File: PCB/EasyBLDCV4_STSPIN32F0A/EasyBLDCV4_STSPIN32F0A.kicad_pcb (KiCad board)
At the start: 4 copper layers, 72.4 x 45.7 mm, 74 parts, among them J1 10159560-A00221RLF, J2 Conn_01x05_Pin, Q1 CSD17573Q5B, Q2 CSD17573Q5B, Q3 CSD17573Q5B, Q4 CSD17573Q5B, Q5 CSD17573Q5B, Q6 CSD17573Q5B, U1 MCF8329A1IREER

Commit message: Started Layout
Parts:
- removed JP1, JP2: SolderJumper_3_Bridged12, Jumper:SolderJumper-3_P1.3mm_Bridged12_RoundedPad1.0x1.5mm_NumberLabels
- removed Q4, Q5, Q6: CSD17573Q5B, EasyBLDC:DNK0008A
- removed TP10, TP11, TP12, TP13, TP14, TP15, TP16, TP3, TP4, TP5, TP6, TP7, TP8, TP9: TestPoint, TestPoint:TestPoint_Pad_D1.5mm
- added C19: 1u, Capacitor_SMD:C_0402_1005Metric, F.Cu at (163.3, 76.5)
- added C20: 1u, Capacitor_SMD:C_0402_1005Metric, F.Cu at (161.3, 76.5)
- added C21: 1u, Capacitor_SMD:C_0402_1005Metric, F.Cu at (159.3, 76.5)
- added D4: GREEN, LED_SMD:LED_0603_1608Metric, F.Cu at (133.1, 102.3)
- added L1: 22u, Inductor_SMD:L_0805_2012Metric, F.Cu at (153.0, 61.0)
- added R23: 10k, Resistor_SMD:R_0402_1005Metric, F.Cu at (155.3, 71.2)
- added U2: STSPIN32F0A, EasyBLDC:IC_STSPIN32F0A, F.Cu at (161.2, 70.8)
- C1: value 10u -> 47u; footprint Capacitor_SMD:CP_Elec_5x5.3 -> Capacitor_SMD:C_1206_3216Metric
- C10, C11, C9: value 1u -> 47u; footprint Capacitor_SMD:C_0603_1608Metric -> Capacitor_SMD:C_1206_3216Metric
- C12: footprint Capacitor_SMD:C_0603_1608Metric -> Capacitor_SMD:C_0805_2012Metric
- C13: value 0.1u -> 100n; footprint Capacitor_SMD:C_0603_1608Metric -> Capacitor_SMD:C_0402_1005Metric
- C14: value 470n -> 22u
- C15: value 1u -> 100n; footprint Capacitor_SMD:C_0603_1608Metric -> Capacitor_SMD:C_0402_1005Metric
- C16: value 10u -> 100n; footprint Capacitor_SMD:C_0603_1608Metric -> Capacitor_SMD:C_0402_1005Metric
- C17: value 10u -> 100n; footprint Capacitor_SMD:C_2220_5750Metric -> Capacitor_SMD:C_0402_1005Metric
- C18: footprint Capacitor_SMD:C_0603_1608Metric -> Capacitor_SMD:C_0402_1005Metric
- C2: value 220u -> 47u; footprint Capacitor_SMD:CP_Elec_10x10.5 -> Capacitor_SMD:C_1206_3216Metric
- C3, C7: value 0.01u -> 47u; footprint Capacitor_SMD:C_0805_2012Metric -> Capacitor_SMD:C_1206_3216Metric
- C4: value 4.7u -> 100n; footprint Capacitor_SMD:C_1210_3225Metric -> Capacitor_SMD:C_0402_1005Metric
- C5: value 0.01u -> 100n; footprint Capacitor_SMD:C_0805_2012Metric -> Capacitor_SMD:C_0402_1005Metric
- C6, C8: value 4.7u -> 47u; footprint Capacitor_SMD:C_1210_3225Metric -> Capacitor_SMD:C_1206_3216Metric
- D1, D2: value GREEN -> D; footprint LED_SMD:LED_0805_2012Metric -> Diode_SMD:D_0402_1005Metric
- D3: value RED -> GREEN; footprint LED_SMD:LED_0805_2012Metric -> LED_SMD:LED_0603_1608Metric
- J2: value Conn_01x05_Pin -> STLINK-V3MINIE-EDGE; footprint Connector_PinSocket_2.54mm:PinSocket_1x05_P2.54mm_Vertical -> EasyBLDC:STLINK-V3MINIE-EDGE
- Q1, Q2, Q3: value CSD17573Q5B -> IAUC60N04S6N031HATMA1; footprint EasyBLDC:DNK0008A -> EasyBLDC:PG-TDSON-8-56
- R1, R2, R3, R4: value 10k -> 33; footprint Resistor_SMD:R_0603_1608Metric -> Resistor_SMD:R_0402_1005Metric
- R10: value 10 -> 1k; footprint Resistor_SMD:R_0603_1608Metric -> Resistor_SMD:R_0402_1005Metric
- R11, R13, R18: value 0 -> 10k; footprint Resistor_SMD:R_0603_1608Metric -> Resistor_SMD:R_0402_1005Metric
- R12: value 0.001 -> 10k; footprint Resistor_SMD:R_2512_6332Metric -> Resistor_SMD:R_0402_1005Metric
- R14: value 5.1k -> 0.001; footprint Resistor_SMD:R_0603_1608Metric -> Resistor_SMD:R_2512_6332Metric
- R15, R17: value 5.1k -> 2.2k; footprint Resistor_SMD:R_0603_1608Metric -> Resistor_SMD:R_0402_1005Metric
- R16: value 0 -> 2.2k; footprint Resistor_SMD:R_0603_1608Metric -> Resistor_SMD:R_0402_1005Metric
- R19: value 5.1k -> 1k; footprint Resistor_SMD:R_0603_1608Metric -> Resistor_SMD:R_0402_1005Metric
- R20: value 2k -> 100k; footprint Resistor_SMD:R_0603_1608Metric -> Resistor_SMD:R_0402_1005Metric
- R21: value 890 -> 10k; footprint Resistor_SMD:R_0603_1608Metric -> Resistor_SMD:R_0201_0603Metric
- R22: value 890 -> 2.2k; footprint Resistor_SMD:R_0603_1608Metric -> Resistor_SMD:R_0201_0603Metric
- R5, R6: value 10 -> 33; footprint Resistor_SMD:R_0603_1608Metric -> Resistor_SMD:R_0402_1005Metric
- R7, R8, R9: value 10 -> 10k; footprint Resistor_SMD:R_0603_1608Metric -> Resistor_SMD:R_0402_1005Metric
- TP1: value TestPoint -> TELEMETRY; footprint TestPoint:TestPoint_Pad_D1.5mm -> TestPoint:TestPoint_Pad_D3.0mm
- TP2: footprint TestPoint:TestPoint_Pad_D1.5mm -> TestPoint:TestPoint_Pad_D3.0mm
- U1: value MCF8329A1IREER -> INA180A1IDBVR; footprint EasyBLDC:WQFN36_REE_TEX -> EasyBLDC:DBV0005A_N
- moved R2 136.5 mm to (158.8, 91.0)
- moved R14 132.6 mm to (164.0, 99.5)
- moved R4 131.9 mm to (157.2, 78.2), turned to 0 degrees
- moved J2 128.5 mm to (176.5, 65.5)
- moved C14 127.7 mm to (167.2, 75.2), turned to -90 degrees
- moved C15 127.6 mm to (167.3, 67.0), turned to 0 degrees
- moved C17 127.5 mm to (160.5, 63.5)
- moved D1 125.4 mm to (159.2, 63.5), turned to 90 degrees
- moved R18 122.4 mm to (167.3, 72.0), turned to 180 degrees
- moved R16 122.1 mm to (166.8, 63.5)
- moved C18 122.0 mm to (163.0, 63.5), turned to -90 degrees
- moved R20 121.6 mm to (155.3, 70.0), turned to 0 degrees
- moved C13 121.0 mm to (161.8, 63.5), turned to 90 degrees
- moved U1 120.4 mm to (157.4, 99.5), turned to 180 degrees
- moved C10 118.7 mm to (158.5, 94.0), turned to -90 degrees
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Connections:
- C10 pad 1: Net-(U1A-SHB) -> PVDD
- C10 pad 2: BSTB -> /Power Stage/SENSE
- C11 pad 1: Net-(U1A-SHC) -> PVDD
- C11 pad 2: BSTC -> /Power Stage/SENSE
- C12 pad 1: AVDD -> GND
- C12 pad 2: GND -> Net-(U2-VREG12)
- C13 pad 1: AVDD -> NRST
- C14 pad 1: Net-(U1B-CPH) -> AVDD
- C14 pad 2: Net-(U1B-CPL) -> GND
- C15 pad 1: Net-(U1B-DVDD) -> AVDD
- C16 pad 1: Net-(U1B-GVDD) -> AVDD
- C18 pad 1: PVDD -> GND
- C18 pad 2: GND -> Net-(U2-VREG12)
- C3 pad 2: LSS -> GND
- C4 pad 1: PVDD -> AVDD
- C5 pad 1: PVDD -> CURRENT_SENSE
- C5 pad 2: LSS -> GND
- C6 pad 2: GND -> /Power Stage/SENSE
- C7 pad 2: LSS -> /Power Stage/SENSE
- C8 pad 2: GND -> /Power Stage/SENSE
- C9 pad 1: Net-(U1A-SHA) -> PVDD
- C9 pad 2: BSTA -> /Power Stage/SENSE
- D1 pad 2: PVDD -> GND
- D2 pad 1: Net-(D2-K) -> AVDD
- D2 pad 2: AVDD -> SIGNAL
- D3 pad 2: AVDD -> PVDD
- J2 pad 1: GND -> unconnected-(J2-Reserved-Pad1)
- J2 pad 2: FGOUT -> unconnected-(J2-T_JTDI/NC-Pad2)
- J2 pad 3: nFAULT -> SWDIO
- J2 pad 4: MCX_SDA -> SWCLK
- J2 pad 5: MCX_SCL -> unconnected-(J2-T_JTDO/T_SWO-Pad5)
- Q1 pad 1: MOT_A -> Net-(Q1-G1)
- Q1 pad 4: Net-(Q1-G) -> Net-(Q1-G2)
- Q1 pad 7: PVDD -> /Power Stage/SENSE
- Q1 pad 8: PVDD -> /Power Stage/SENSE
- Q2 pad 1: LSS -> Net-(Q2-G1)
- Q2 pad 2: LSS -> MOT_B
- Q2 pad 3: LSS -> MOT_B
- Q2 pad 4: Net-(Q2-G) -> Net-(Q2-G2)
- Q2 pad 5: MOT_A -> PVDD
- Q2 pad 6: MOT_A -> PVDD
- Q2 pad 7: MOT_A -> /Power Stage/SENSE
- Q2 pad 8: MOT_A -> /Power Stage/SENSE
- Q3 pad 1: MOT_B -> Net-(Q3-G1)
- Q3 pad 2: MOT_B -> MOT_C
- Q3 pad 3: MOT_B -> MOT_C
- Q3 pad 4: Net-(Q3-G) -> Net-(Q3-G2)
- Q3 pad 7: PVDD -> /Power Stage/SENSE
- Q3 pad 8: PVDD -> /Power Stage/SENSE
- R1 pad 1: GND -> GH_A
- R1 pad 2: DRVOFF -> Net-(Q1-G1)
- R10 pad 1: GL_C -> Net-(U1-OUT)
- R10 pad 2: Net-(Q6-G) -> CURRENT_SENSE
- R11 pad 1: LSS -> MOT_A
- R11 pad 2: SP -> BEMF_A
- R12 pad 1: GND -> MOT_B
- R12 pad 2: LSS -> BEMF_B
- R13 pad 1: GND -> MOT_C
- R13 pad 2: SN -> BEMF_C
- R14 pad 1: MCX_SCL -> GND
- R14 pad 2: AVDD -> /Power Stage/SENSE
- R15 pad 1: FGOUT -> GND
- R15 pad 2: AVDD -> BEMF_A
- R16 pad 1: MCX_SCL -> GND
- R16 pad 2: Net-(U1A-SCL) -> BEMF_B
- R17 pad 1: MCX_SDA -> GND
- R17 pad 2: AVDD -> BEMF_C
- R18 pad 1: MCX_SDA -> GND
- R18 pad 2: Net-(U1A-SDA) -> Net-(U2-BOOT0)
- R19 pad 1: nFAULT -> SIGNAL
- R19 pad 2: AVDD -> Net-(U2-PA2)
- R2 pad 1: Net-(JP2-B) -> GH_B
- R2 pad 2: AVDD -> Net-(Q2-G1)
- R20 pad 1: GND -> PVDD
- R20 pad 2: Net-(D1-K) -> VOLT_SENSE
- R21 pad 2: Net-(D2-K) -> Net-(D3-K)
- R22 pad 1: nFAULT -> GND
- R22 pad 2: Net-(D3-K) -> Net-(D4-K)
- R3 pad 1: GND -> GH_C
- R3 pad 2: BRAKE -> Net-(Q3-G1)
- R4 pad 1: GND -> GL_A
- R4 pad 2: Net-(JP2-A) -> Net-(Q1-G2)
- R5 pad 1: GH_A -> GL_B
- R5 pad 2: Net-(Q1-G) -> Net-(Q2-G2)
- R6 pad 1: GH_B -> GL_C
- R6 pad 2: Net-(Q3-G) -> Net-(Q3-G2)
- R7 pad 1: GH_C -> BEMF_A
- R7 pad 2: Net-(Q5-G) -> BEMF_COMMON
- R8 pad 1: GL_A -> BEMF_B
- R8 pad 2: Net-(Q2-G) -> BEMF_COMMON
- R9 pad 1: GL_B -> BEMF_C
- R9 pad 2: Net-(Q4-G) -> BEMF_COMMON
- TP1 pad 1: Net-(Q1-G) -> Net-(U2-PB6)
- TP2 pad 1: Net-(Q3-G) -> Net-(U2-PB7)
- U1 pad 1: GND -> Net-(U1-OUT)
- U1 pad 2: AVDD -> GND
- U1 pad 3: GCTRL -> /Power Stage/SENSE
- U1 pad 5: PVDD -> AVDD
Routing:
- net INPUT: track 117.7 -> 0.00 mm
- net AVDD: track 60.6 -> 7.31 mm, vias 6 -> 0
- net GH_A: track 45.2 -> 0.00 mm, vias 2 -> 0
- net GND: track 32.6 -> 2.95 mm, vias 157 -> 70
- net PVDD: track 52.0 -> 22.6 mm, vias 117 -> 30
- net GL_C: track 29.1 -> 0.00 mm
- net Net-(U1B-DVDD): track 28.6 -> 0.00 mm
- net nFAULT: track 27.1 -> 0.00 mm
- net SN: track 24.9 -> 0.00 mm
- net Net-(Q3-G): track 22.6 -> 0.00 mm, vias 2 -> 0
- net Net-(Q5-G): track 22.0 -> 0.00 mm, vias 2 -> 0
- net SPEED/WAKE: track 21.4 -> 0.00 mm, vias 2 -> 0
- net GL_A: track 21.1 -> 0.00 mm, vias 2 -> 0
- net FGOUT: track 20.8 -> 0.00 mm
- net GH_B: track 18.4 -> 0.00 mm, vias 2 -> 0
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- removed copper zone on F.Cu, net LSS

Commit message: More layout progress
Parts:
- removed H1, H2, H3, H4: M2.5, MountingHole:MountingHole_2.7mm_M2.5_ISO7380
- moved TP1 47.6 mm to (166.0, 47.5)
- moved TP2 47.6 mm to (158.0, 46.2)
- moved C3 25.0 mm to (166.0, 76.8), turned to 180 degrees
- moved C1 22.9 mm to (166.0, 71.2)
- moved C2 20.9 mm to (166.0, 74.0), turned to 180 degrees
- moved C14 20.6 mm to (149.0, 65.8)
- moved D3 17.3 mm to (146.0, 94.5)
- moved R6 17.0 mm to (141.5, 98.1)
- moved D4 16.8 mm to (148.0, 94.5)
- moved R21 16.4 mm to (145.2, 97.4)
- moved R22 15.3 mm to (146.8, 97.8)
- moved R2 13.7 mm to (151.0, 79.8), turned to -90 degrees
- moved C5 13.0 mm to (136.5, 99.9)
- moved R1 12.4 mm to (146.0, 79.2)
- moved R5 12.4 mm to (148.5, 79.5)
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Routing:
- net PVDD: track 22.6 -> 4.13 mm, vias 30 -> 67
- net GND: track 2.95 -> 17.7 mm, vias 70 -> 67
- net /Power Stage/SENSE: track 0.00 -> 14.2 mm
- net unconnected-(J2-T_VCP_TX-Pad8): track 11.5 -> 0.00 mm
- net Net-(U2-VREG12): track 0.00 -> 6.49 mm
- net Net-(D1-K): track 0.00 -> 5.39 mm
- net BEMF_A: track 0.00 -> 5.07 mm
- net /MCU/OP3O: track 0.00 -> 3.59 mm
- net GL_A: track 0.00 -> 3.53 mm
- net NRST: track 0.00 -> 3.40 mm
- net AVDD: track 7.31 -> 10.4 mm
- net Net-(U2-BOOT0): track 0.00 -> 2.55 mm
- net BEMF_COMMON: track 3.44 -> 5.90 mm
- net Net-(U2-VBOOTU): track 0.00 -> 2.29 mm
- net MOT_C: track 0.00 -> 1.97 mm
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- added copper zone on F.Cu, net /Power Stage/SENSE
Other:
- board size 72.4 x 45.7 mm -> 31.4 x 39.2 mm

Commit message: Layout almost final
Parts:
- moved R22 39.5 mm to (174.7, 69.8), turned to 180 degrees
- moved R21 37.6 mm to (170.7, 69.8), turned to 180 degrees
- moved D4 35.6 mm to (174.8, 71.0), turned to 180 degrees
- moved D3 34.1 mm to (170.8, 71.0), turned to 180 degrees
- moved R5 17.5 mm to (148.8, 97.0)
- moved R6 15.9 mm to (148.8, 84.0), turned to -90 degrees
- moved TP1 10.3 mm to (173.0, 55.0)
- moved TP2 10.0 mm to (158.8, 56.2)
- moved R2 7.34 mm to (148.8, 86.7)
- moved R1 4.50 mm to (146.0, 83.8), turned to -90 degrees
- moved R3 3.80 mm to (148.8, 81.2)
- moved R4 2.75 mm to (161.8, 74.8)
- moved J2 1.52 mm to (171.0, 63.0)
- moved R8 1.42 mm to (164.8, 66.3)
- moved R16 1.28 mm to (163.6, 66.3)
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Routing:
- net AVDD: track 10.4 -> 84.2 mm, vias 0 -> 4
- net MOT_B: track 1.64 -> 45.0 mm, vias 0 -> 2
- net Net-(Q3-G1): track 0.00 -> 35.1 mm, vias 0 -> 2
- net Net-(Q3-G2): track 0.00 -> 34.1 mm, vias 0 -> 2
- net Net-(Q2-G1): track 0.00 -> 31.2 mm, vias 0 -> 2
- net PVDD: track 4.13 -> 31.5 mm, vias 67 -> 73
- net BEMF_COMMON: track 5.90 -> 27.7 mm, vias 0 -> 3
- net NRST: track 3.40 -> 25.1 mm, vias 0 -> 3
- net SWDIO: track 0.00 -> 20.2 mm, vias 0 -> 2
- net SWCLK: track 0.00 -> 18.0 mm, vias 0 -> 2
- net GH_B: track 0.00 -> 14.5 mm
- net GL_C: track 0.00 -> 11.3 mm
- net GND: track 17.7 -> 27.2 mm, vias 67 -> 89
- net (no net): track 0.07 -> 8.71 mm
- net Net-(Q1-G2): track 0.00 -> 7.58 mm
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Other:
- board size 31.4 x 39.2 mm -> 30.4 x 39.7 mm

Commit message: Design finished, ready for review
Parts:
- TP1, TP2: footprint TestPoint:TestPoint_Pad_D3.0mm -> TestPoint:TestPoint_Pad_D1.5mm
- moved TP1 37.5 mm to (141.4, 75.2)
- moved C5 33.4 mm to (142.4, 67.0)
- moved TP2 18.5 mm to (153.7, 74.0)
- moved C4 14.3 mm to (160.7, 96.2), turned to -90 degrees
- moved R5 11.0 mm to (141.2, 89.0), turned to -90 degrees
- moved R10 9.98 mm to (140.2, 68.0), turned to 90 degrees
- moved U1 8.47 mm to (157.8, 96.2)
- moved C15 8.24 mm to (154.3, 65.2)
- moved C20 8.24 mm to (148.0, 74.8)
- moved C6 8.24 mm to (150.6, 78.2)
- moved D2 8.24 mm to (142.3, 64.5)
- moved J1 8.24 mm to (165.0, 83.6)
- moved R11 8.24 mm to (154.3, 67.8)
- moved R13 8.24 mm to (142.3, 73.5)
- moved R15 8.24 mm to (154.3, 69.0)
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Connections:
- J1 pad S1: GND -> unconnected-(J1-SHIELD-PadS1)
- J1 pad S2: GND -> unconnected-(J1-SHIELD__1-PadS2)
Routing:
- net Net-(U1-OUT): track 0.00 -> 50.0 mm
- net MOT_C: track 5.51 -> 50.9 mm, vias 0 -> 2
- net MOT_A: track 4.82 -> 41.2 mm, vias 1 -> 3
- net Net-(Q1-G1): track 1.67 -> 31.5 mm, vias 1 -> 2
- net Net-(Q2-G2): track 1.28 -> 28.9 mm, vias 1 -> 2
- net GL_B: track 2.32 -> 22.8 mm, vias 1 -> 2
- net MOT_B: track 45.0 -> 64.6 mm, vias 2 -> 4
- net GH_A: track 1.38 -> 19.9 mm, vias 1 -> 2
- net Net-(U2-PB6): track 1.09 -> 14.5 mm, vias 1 -> 2
- net (no net): track 8.71 -> 0.07 mm
- net Net-(U2-PB7): track 0.00 -> 6.48 mm, vias 0 -> 2
- net GND: track 27.2 -> 33.7 mm, vias 89 -> 90
- net GH_C: track 1.81 -> 8.01 mm, vias 1 -> 2
- net CURRENT_SENSE: track 2.30 -> 5.47 mm, vias 1 -> 0
- net Net-(Q2-G1): track 31.2 -> 34.3 mm
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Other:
- board size 30.4 x 39.7 mm -> 31 x 40 mm
- board text removed: "EasyBLDC REV2"

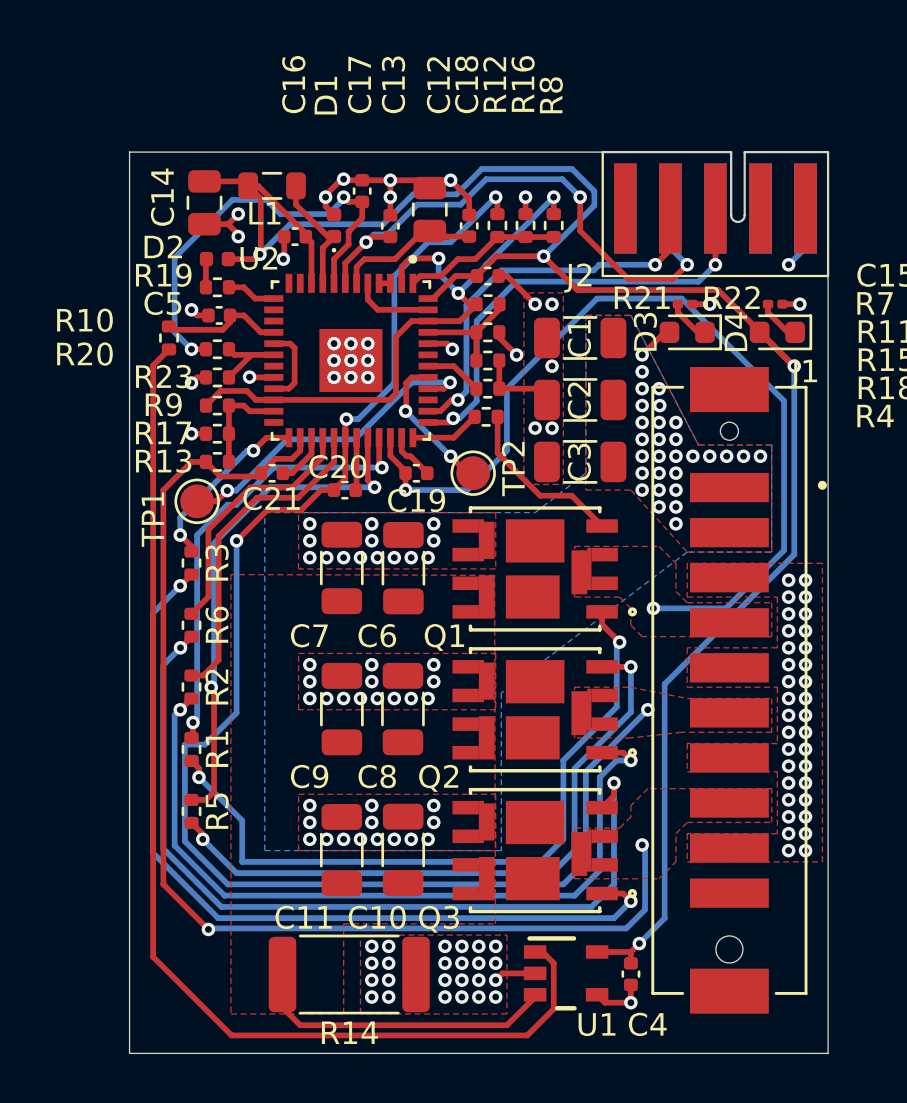
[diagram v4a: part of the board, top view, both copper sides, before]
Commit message: Fixed DRC Errors. Ready for review
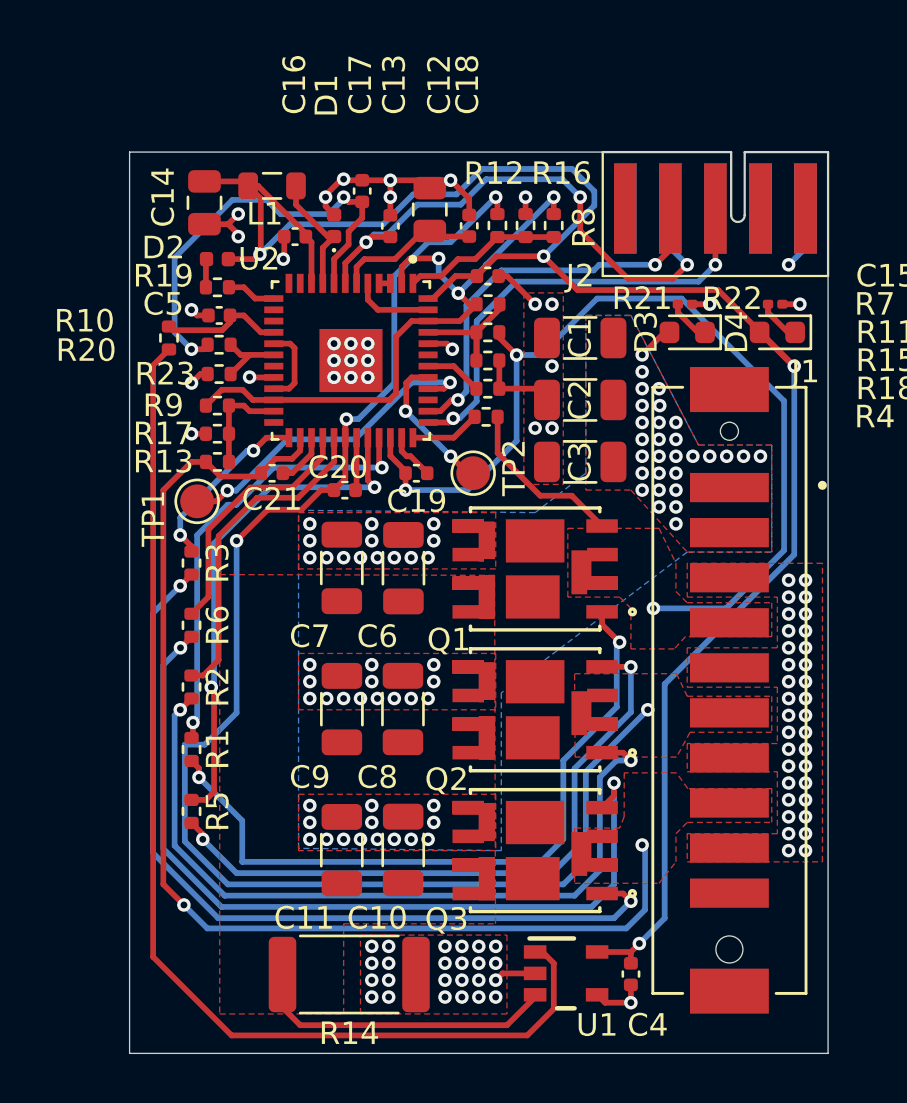
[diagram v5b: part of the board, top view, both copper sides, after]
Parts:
- Q1, Q2, Q3: footprint EasyBLDC:PG-TDSON-8-56 -> EasyBLDC:PG-TDSON-8-56-2
- moved R20 0.21 mm to (142.4, 68.3)
- moved R23 0.17 mm to (142.4, 69.6)
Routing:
- net MOT_A: track 41.2 -> 41.9 mm

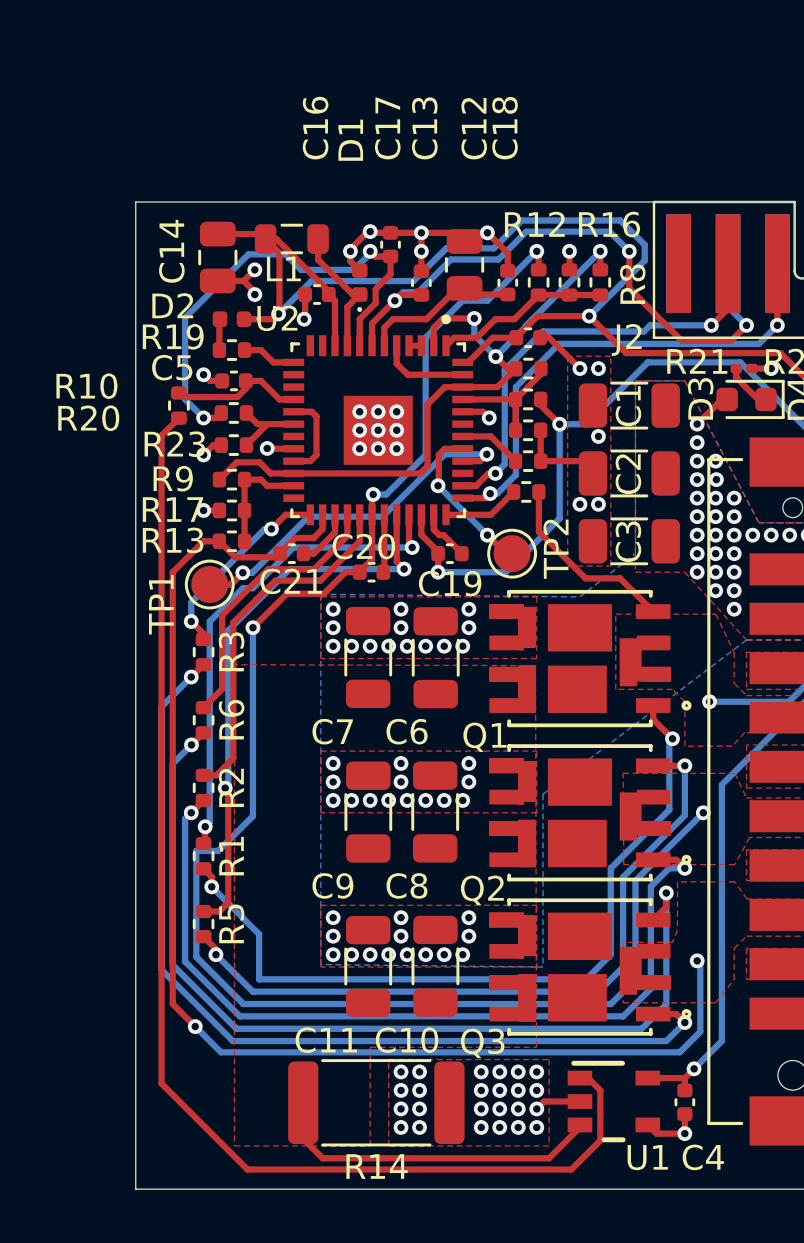
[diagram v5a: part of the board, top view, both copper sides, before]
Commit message: Updated Board According to Dirk Kaisers Review
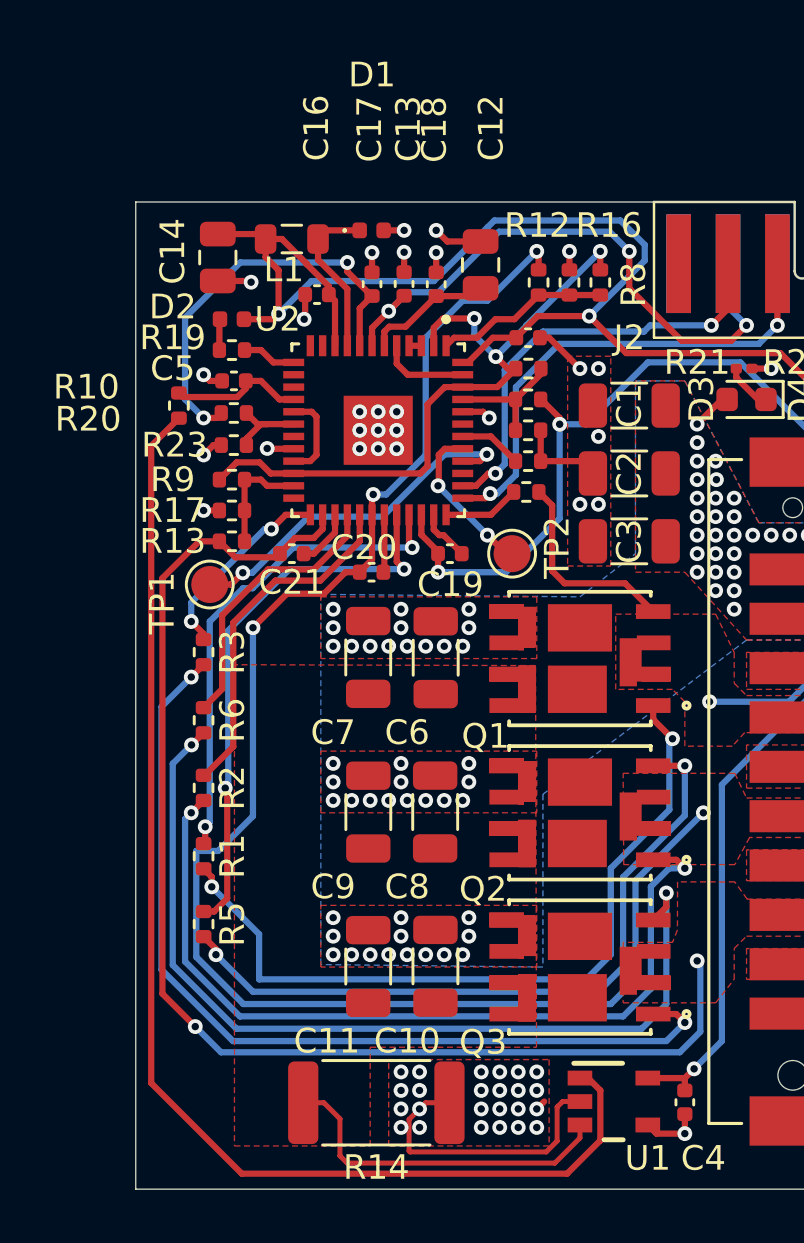
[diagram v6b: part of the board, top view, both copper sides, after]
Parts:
- moved C18 2.90 mm to (150.6, 63.1)
- moved D1 2.17 mm to (148.0, 60.9), turned to 0 degrees
- moved C17 1.77 mm to (148.0, 63.1)
- moved C13 0.70 mm to (149.3, 63.1)
- moved C12 0.65 mm to (152.4, 62.3)
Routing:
- net GND: track 33.8 -> 38.3 mm, vias 90 -> 89
- net PVDD: track 31.0 -> 35.2 mm
- net /Power Stage/SENSE: track 13.6 -> 15.1 mm
- net Net-(U2-VREG12): track 6.49 -> 5.20 mm
- net Net-(D1-K): track 5.39 -> 6.65 mm
- net NRST: track 24.9 -> 24.2 mm
- net Net-(U1-OUT): track 50.0 -> 50.7 mm
- net Net-(Q1-G2): track 7.58 -> 8.20 mm

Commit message: Updated bom
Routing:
- net GH_C: track 8.01 -> 8.59 mm
- net GND: track 38.3 -> 38.8 mm
- net MOT_B: track 64.6 -> 64.1 mm
